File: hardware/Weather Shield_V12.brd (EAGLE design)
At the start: 53.3 x 59.7 mm, 52 parts, among them J1 GP-735, Q1 200mA/50V, Q2 200mA/50V, U1 ARDUINO_R3_SHIELD, U3 ALS-PT19, U4 MPL3115A2LGA8, U5 SI7021, U6 3.3V/150mA

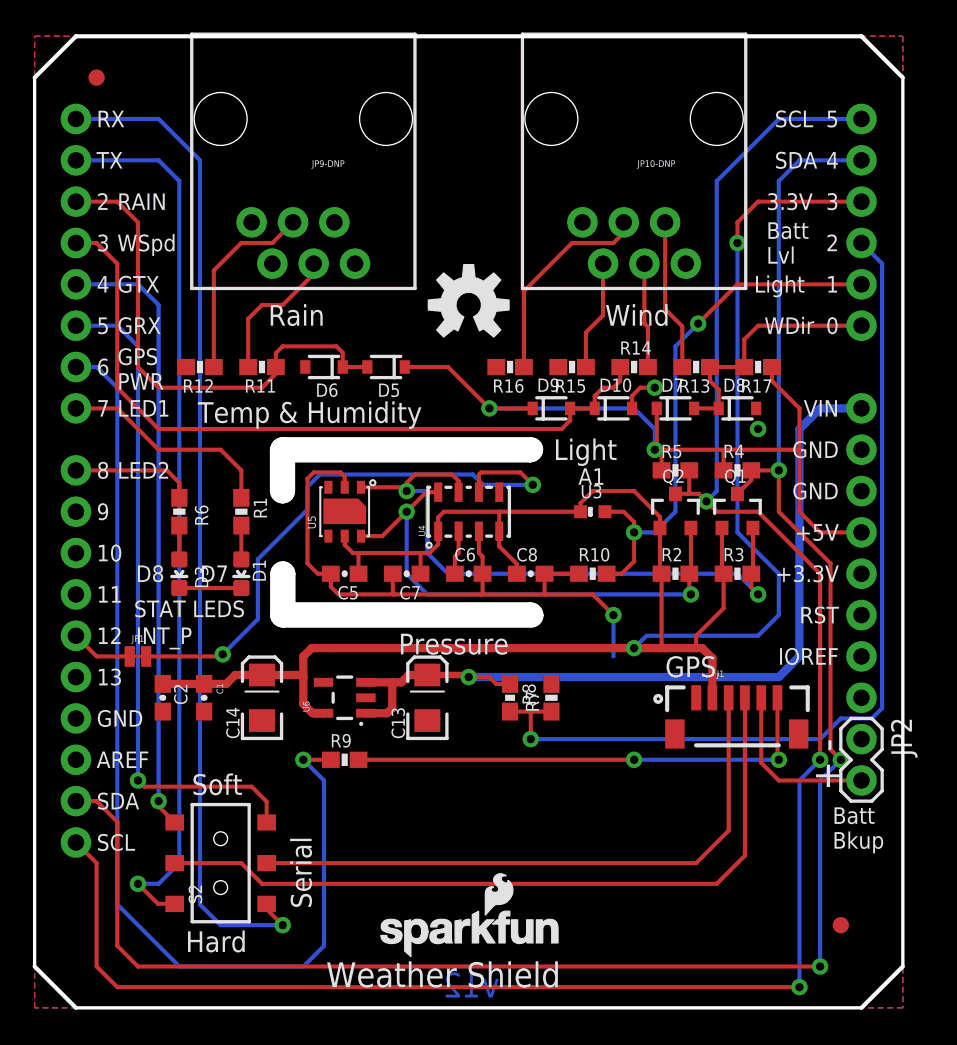
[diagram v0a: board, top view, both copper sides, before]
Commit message: Slight modifications before final review
Moved logos to avoid cover up by GPS. Moved GPS backup batter
connection. Change jumper on D12 to NO instead of NC.
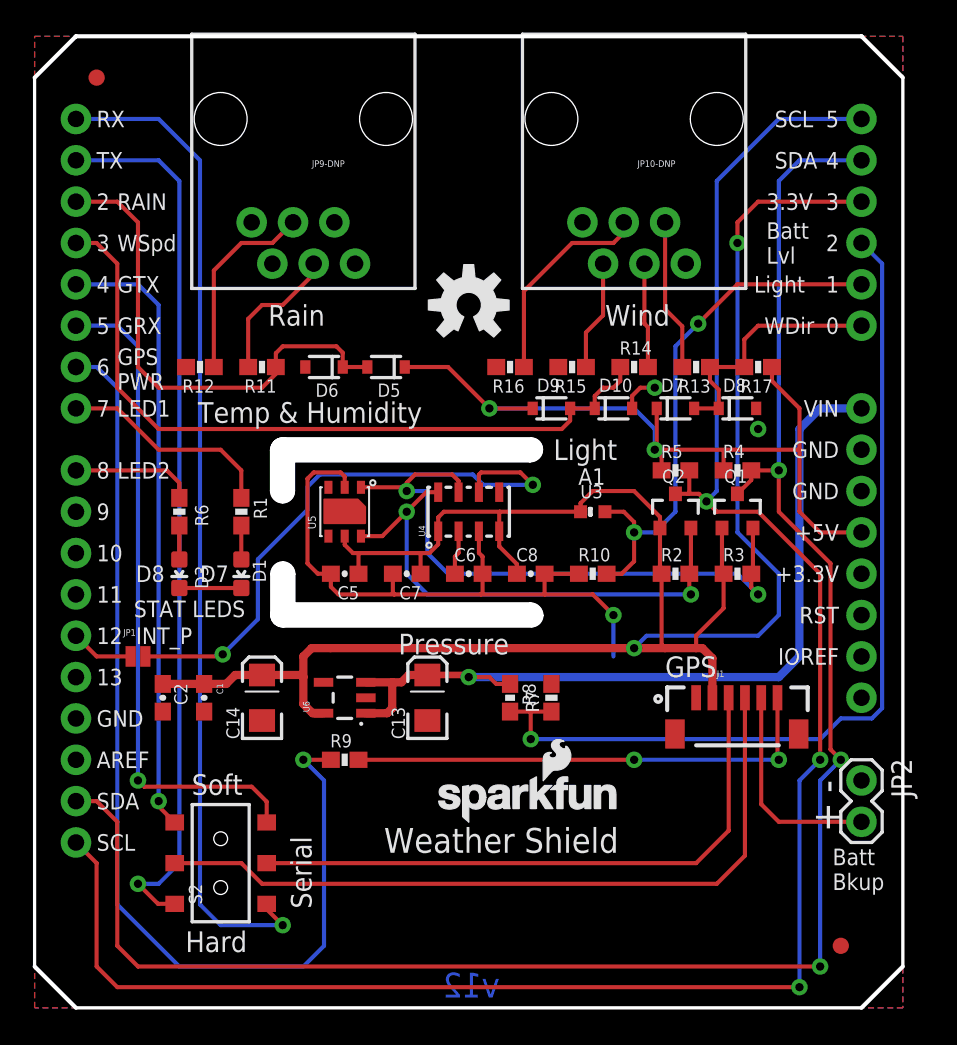
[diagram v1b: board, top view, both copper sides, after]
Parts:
- JP1: value (none) -> JUMPER-PAD-2-NO; device SparkFun-Passives:PAD-JUMPER-2-NC_BY_TRACE_NO_SILK -> SparkFun-Passives:PAD-JUMPER-2-NO_NO_SILK
- moved LOGO2 8.99 mm to (24.4, 11.3)
- moved JP2 2.54 mm to (50.8, 14.0)
- moved FD1 1.27 mm to (49.5, 3.81)
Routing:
- net V_BATT: track 10.6 -> 13.1 mm
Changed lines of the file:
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@@
 <layer number="29" name="tStop" color="7" fill="3" visible="yes" active="yes"/>
 <layer number="30" name="bStop" color="7" fill="6" visible="no" active="yes"/>
-<layer number="31" name="tCream" color="7" fill="4" visible="no" active="yes"/>
+<layer number="31" name="tCream" color="7" fill="4" visible="yes" active="yes"/>
 <layer number="32" name="bCream" color="7" fill="5" visible="no" active="yes"/>
 <layer number="33" name="tFinish" color="6" fill="3" visible="no" active="yes"/>
@@
 <layer number="47" name="Measures" color="7" fill="1" visible="no" active="yes"/>
 <layer number="48" name="Document" color="7" fill="1" visible="no" active="yes"/>
-<layer number="49" name="Reference" color="7" fill="1" visible="no" active="yes"/>
+<layer number="49" name="Reference" color="7" fill="1" visible="yes" active="yes"/>
 <layer number="50" name="dxf" color="7" fill="1" visible="no" active="yes"/>
 <layer number="51" name="tDocu" color="6" fill="1" visible="yes" active="yes"/>
@@
 <wire x1="53.34" y1="2.54" x2="53.34" y2="57.15" width="0.2032" layer="20"/>
 <wire x1="0" y1="57.15" x2="0" y2="2.54" width="0.2032" layer="20"/>
-<text x="17.907" y="1.27" size="1.524" layer="21" font="vector" ratio="15">Weather Shield</text>
+<text x="21.463" y="9.525" size="1.524" layer="21" font="vector" ratio="15">Weather Shield</text>
 <text x="22.86" y="-24.13" size="1.778" layer="51" font="vector" ratio="15">N. Seidle</text>
 <text x="22.352" y="21.717" size="1.27" layer="21" font="vector" ratio="15">Pressure</text>
@@
 <rectangle x1="12.7" y1="22.86" x2="39.37" y2="35.56" layer="41"/>
 <rectangle x1="12.7" y1="22.86" x2="39.37" y2="35.56" layer="42"/>
-<text x="49.022" y="9.779" size="1.016" layer="21" font="vector" ratio="15">Batt
+<text x="49.022" y="7.239" size="1.016" layer="21" font="vector" ratio="15">Batt
 Bkup</text>
-<text x="49.53" y="13.335" size="1.778" layer="21" font="vector" ratio="15" rot="R90">+</text>
-<text x="49.53" y="15.748" size="1.778" layer="21" font="vector" ratio="15" rot="R90">-</text>
+<text x="49.53" y="10.795" size="1.778" layer="21" font="vector" ratio="15" rot="R90">+</text>
+<text x="49.53" y="13.208" size="1.778" layer="21" font="vector" ratio="15" rot="R90">-</text>
 <wire x1="15.24" y1="31.75" x2="15.24" y2="34.29" width="1.524" layer="46"/>
 <wire x1="15.24" y1="34.29" x2="30.48" y2="34.29" width="1.524" layer="46"/>
@@
 <attribute name="PROD_ID" value="RES-07856" x="29.21" y="39.37" size="1.778" layer="27" rot="R180" display="off"/>
 </element>
-<element name="LOGO2" library="SparkFun-Aesthetics" package="SFE_LOGO_NAME_FLAME_.1" value="SFE_LOGO_NAME_FLAME.1_INCH" x="20.828" y="3.048"/>
+<element name="LOGO2" library="SparkFun-Aesthetics" package="SFE_LOGO_NAME_FLAME_.1" value="SFE_LOGO_NAME_FLAME.1_INCH" x="24.384" y="11.303"/>
 <element name="R7" library="SparkFun-Resistors" package="0603-RES" value="1K" x="31.75" y="19.05" smashed="yes" rot="R90">
 <attribute name="NAME" x="30.988" y="18.161" size="0.8128" layer="25" font="vector" rot="R90"/>
@@
 <attribute name="PROD_ID" value="RES-07857" x="19.05" y="15.24" size="1.778" layer="27" display="off"/>
 </element>
-<element name="JP2" library="SparkFun-Connectors" package="1X02" value="External Batt Bckup" x="50.8" y="16.51" rot="R270"/>
+<element name="JP2" library="SparkFun-Connectors" package="1X02" value="External Batt Bckup" x="50.8" y="13.97" rot="R270"/>
 <element name="U3" library="SparkFun-Sensors" package="ALS-PT19" value="ALS-PT19" x="34.29" y="30.48" smashed="yes">
 <attribute name="NAME" x="33.528" y="31.3055" size="0.8128" layer="25"/>
@@
 </element>
 <element name="U$2" library="SparkFun-Aesthetics" package="REVISION" value="REVISION" x="2.54" y="-27.94"/>
-<element name="FD1" library="SparkFun-Aesthetics" package="FIDUCIAL-1X2" value="FIDUCIAL1X2" x="49.53" y="5.08"/>
+<element name="FD1" library="SparkFun-Aesthetics" package="FIDUCIAL-1X2" value="FIDUCIAL1X2" x="49.53" y="3.81"/>
 <element name="FD2" library="SparkFun-Aesthetics" package="FIDUCIAL-1X2" value="FIDUCIAL1X2" x="3.81" y="57.15"/>
-<element name="JP1" library="SparkFun-Passives" package="PAD-JUMPER-2-NC_BY_TRACE_NO_SILK" value="" x="6.35" y="21.59"/>
+<element name="JP1" library="SparkFun-Passives" package="PAD-JUMPER-2-NO_NO_SILK" value="JUMPER-PAD-2-NO" x="6.35" y="21.59"/>
 <element name="U6" library="SparkFun-PowerIC" package="SOT23-5" value="3.3V/150mA" x="19.05" y="19.05" rot="R90">
 <attribute name="PROD_ID" value="VREG-00822" x="19.05" y="19.05" size="1.778" layer="27" font="vector" ratio="15" rot="R90" display="off"/>
@@
 <contactref element="JP1" pad="2"/>
 <wire x1="11.557" y1="21.717" x2="11.43" y2="21.59" width="0.254" layer="1"/>
-<wire x1="11.43" y1="21.59" x2="6.858" y2="21.59" width="0.254" layer="1"/>
+<wire x1="11.43" y1="21.59" x2="6.8" y2="21.59" width="0.254" layer="1"/>
 </signal>
 <signal name="N$5">
@@
 <contactref element="JP2" pad="2"/>
 <contactref element="J1" pad="5"/>
-<wire x1="44.64" y1="19.05" x2="44.64" y2="15.05" width="0.254" layer="1"/>
-<wire x1="44.64" y1="15.05" x2="45.72" y2="13.97" width="0.254" layer="1"/>
-<wire x1="45.72" y1="13.97" x2="50.8" y2="13.97" width="0.254" layer="1"/>
+<wire x1="44.64" y1="19.05" x2="44.64" y2="12.51" width="0.254" layer="1"/>
+<wire x1="50.8" y1="11.43" x2="45.72" y2="11.43" width="0.254" layer="1"/>
+<wire x1="45.72" y1="11.43" x2="44.64" y2="12.51" width="0.254" layer="1"/>
 </signal>
 <signal name="LIGHT">
@@
 <contactref element="U1" pad="D12"/>
 <contactref element="JP1" pad="1"/>
-<wire x1="5.842" y1="21.59" x2="3.81" y2="21.59" width="0.254" layer="1"/>
+<wire x1="5.9" y1="21.59" x2="3.81" y2="21.59" width="0.254" layer="1"/>
 <wire x1="3.81" y1="21.59" x2="2.54" y2="22.86" width="0.254" layer="1"/>
 </signal>

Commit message: Moved logo
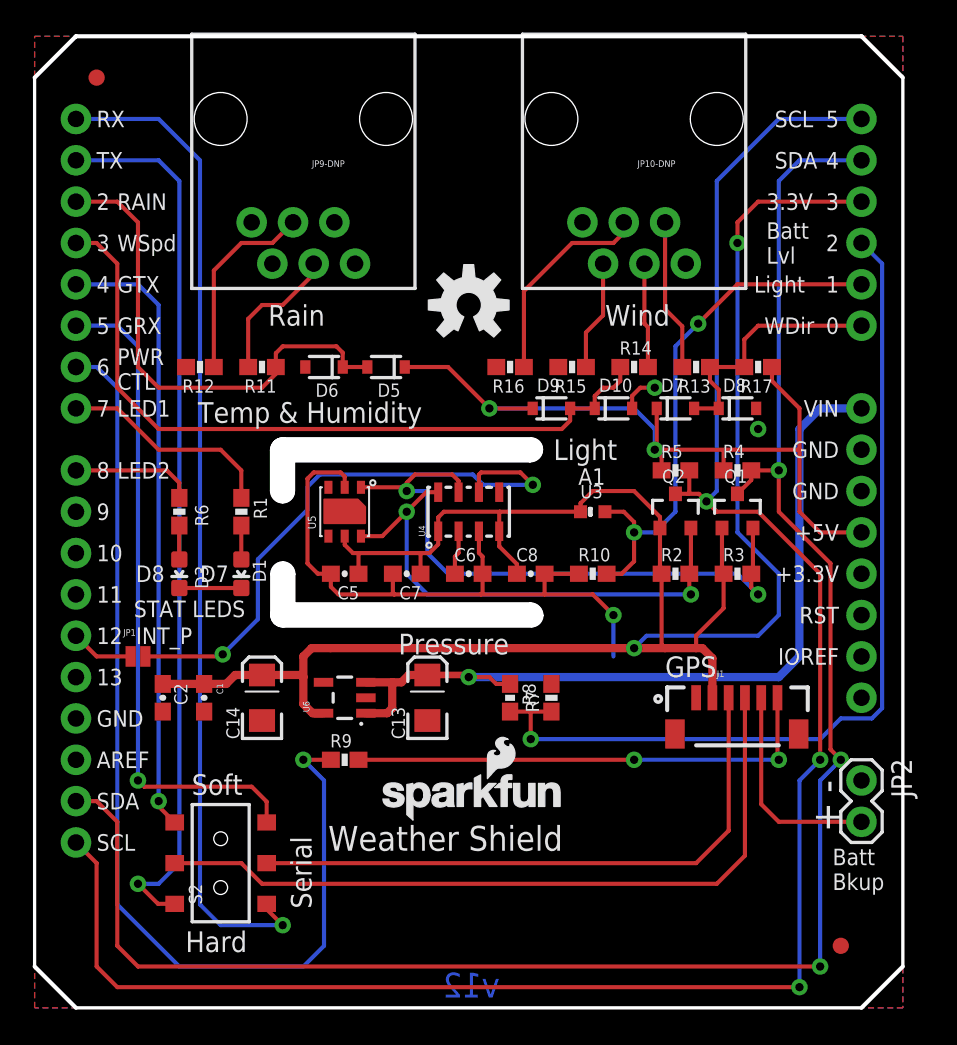
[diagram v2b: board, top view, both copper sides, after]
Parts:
- moved LOGO2 3.43 mm to (21.0, 11.4)
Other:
- board text added: "PWR CTL"
- board text removed: "GPS PWR"
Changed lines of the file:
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@@
 <wire x1="53.34" y1="2.54" x2="53.34" y2="57.15" width="0.2032" layer="20"/>
 <wire x1="0" y1="57.15" x2="0" y2="2.54" width="0.2032" layer="20"/>
-<text x="21.463" y="9.525" size="1.524" layer="21" font="vector" ratio="15">Weather Shield</text>
+<text x="18.034" y="9.652" size="1.524" layer="21" font="vector" ratio="15">Weather Shield</text>
 <text x="22.86" y="-24.13" size="1.778" layer="51" font="vector" ratio="15">N. Seidle</text>
 <text x="22.352" y="21.717" size="1.27" layer="21" font="vector" ratio="15">Pressure</text>
@@
 <text x="6.223" y="26.162" size="1.016" layer="21" font="vector" ratio="15">D8</text>
 <text x="10.16" y="26.162" size="1.016" layer="21" font="vector" ratio="15">D7</text>
-<text x="5.08" y="37.973" size="1.016" layer="21" font="vector" ratio="15">GPS
-PWR</text>
+<text x="5.08" y="37.973" size="1.016" layer="21" font="vector" ratio="15">PWR
+CTL</text>
 <text x="5.08" y="41.402" size="1.016" layer="21" font="vector" ratio="15">GRX</text>
 <text x="5.08" y="43.942" size="1.016" layer="21" font="vector" ratio="15">GTX</text>
@@
 <attribute name="PROD_ID" value="RES-07856" x="29.21" y="39.37" size="1.778" layer="27" rot="R180" display="off"/>
 </element>
-<element name="LOGO2" library="SparkFun-Aesthetics" package="SFE_LOGO_NAME_FLAME_.1" value="SFE_LOGO_NAME_FLAME.1_INCH" x="24.384" y="11.303"/>
+<element name="LOGO2" library="SparkFun-Aesthetics" package="SFE_LOGO_NAME_FLAME_.1" value="SFE_LOGO_NAME_FLAME.1_INCH" x="20.955" y="11.43"/>
 <element name="R7" library="SparkFun-Resistors" package="0603-RES" value="1K" x="31.75" y="19.05" smashed="yes" rot="R90">
 <attribute name="NAME" x="30.988" y="18.161" size="0.8128" layer="25" font="vector" rot="R90"/>

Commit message: Minor Changes after group review for Reds
Fixed text under VREG to have correct info, fixed Eagle error on J1
(GPS Conn), fixed overlapping values, minor silk changes, moved via,
updated HW/SW serial switch text to modern standard .
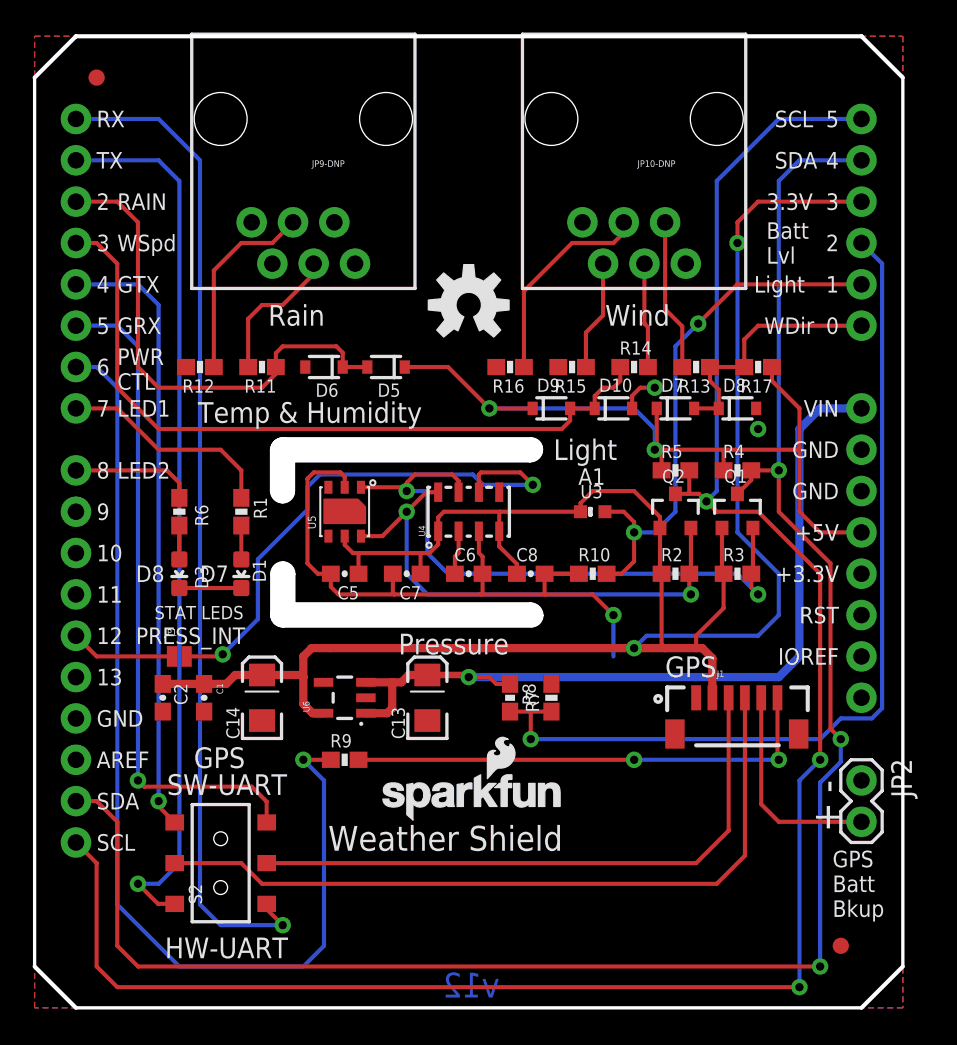
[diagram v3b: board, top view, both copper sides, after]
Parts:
- D10, D5, D6, D7, D8, D9: value 250mA/100V -> (none)
- JP1: value JUMPER-PAD-2-NO -> (none)
- moved JP1 2.54 mm to (8.89, 21.6)
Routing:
- net INT-PRESSURE: track 36.4 -> 33.9 mm
- net N$6: track 3.89 -> 6.43 mm
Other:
- board text added: "GPS Batt Bkup"
- board text added: "HW-UART"
- board text added: "PRESS_INT"
- board text added: "SW-UART"
- board text removed: "Batt Bkup"
- board text removed: "Hard"
- board text removed: "INT_P"
- board text removed: "Serial"
- board text removed: "Soft"

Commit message: Final issue fixes before going out for reds.
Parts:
- D10, D5, D6, D7, D8, D9: value (none) -> 250mA/100V
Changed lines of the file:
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@@
 <text x="38.735" y="20.32" size="1.27" layer="21" font="vector" ratio="15">GPS</text>
 <wire x1="2.54" y1="0" x2="50.8" y2="0" width="0.2032" layer="20"/>
-<wire x1="0" y1="57.15" x2="2.54" y2="59.69" width="0.254" layer="20"/>
-<wire x1="2.54" y1="59.69" x2="50.8" y2="59.69" width="0.254" layer="20"/>
-<wire x1="50.8" y1="59.69" x2="53.34" y2="57.15" width="0.254" layer="20"/>
-<wire x1="53.34" y1="2.54" x2="50.8" y2="0" width="0.254" layer="20"/>
-<wire x1="2.54" y1="0" x2="0" y2="2.54" width="0.254" layer="20"/>
+<wire x1="0" y1="57.15" x2="2.54" y2="59.69" width="0.2032" layer="20"/>
+<wire x1="2.54" y1="59.69" x2="50.8" y2="59.69" width="0.2032" layer="20"/>
+<wire x1="50.8" y1="59.69" x2="53.34" y2="57.15" width="0.2032" layer="20"/>
+<wire x1="53.34" y1="2.54" x2="50.8" y2="0" width="0.2032" layer="20"/>
+<wire x1="2.54" y1="0" x2="0" y2="2.54" width="0.2032" layer="20"/>
 <text x="14.351" y="41.91" size="1.27" layer="21" font="vector" ratio="15">Rain</text>
 <text x="35.052" y="41.91" size="1.27" layer="21" font="vector" ratio="15">Wind</text>
@@
 <attribute name="PROD_ID" value="RES-07856" x="40.64" y="39.37" size="1.778" layer="27" rot="R180" display="off"/>
 </element>
-<element name="D9" library="SparkFun-DiscreteSemi" package="SOD-323" value="" x="31.75" y="36.83" smashed="yes">
+<element name="D9" library="SparkFun-DiscreteSemi" package="SOD-323" value="250mA/100V" x="31.75" y="36.83" smashed="yes">
 <attribute name="NAME" x="30.861" y="37.846" size="0.8128" layer="25"/>
 <attribute name="VALUE" value="250mA/100V" x="30.734" y="35.433" size="0.8128" layer="27"/>
 <attribute name="PROD_ID" value="DIO-09646" x="31.75" y="36.83" size="1.778" layer="27" display="off"/>
 </element>
-<element name="D10" library="SparkFun-DiscreteSemi" package="SOD-323" value="" x="35.56" y="36.83" smashed="yes">
+<element name="D10" library="SparkFun-DiscreteSemi" package="SOD-323" value="250mA/100V" x="35.56" y="36.83" smashed="yes">
 <attribute name="NAME" x="34.671" y="37.846" size="0.8128" layer="25"/>
 <attribute name="VALUE" value="250mA/100V" x="34.544" y="35.433" size="0.8128" layer="27"/>
 <attribute name="PROD_ID" value="DIO-09646" x="35.56" y="36.83" size="1.778" layer="27" display="off"/>
 </element>
-<element name="D7" library="SparkFun-DiscreteSemi" package="SOD-323" value="" x="39.37" y="36.83" smashed="yes">
+<element name="D7" library="SparkFun-DiscreteSemi" package="SOD-323" value="250mA/100V" x="39.37" y="36.83" smashed="yes">
 <attribute name="NAME" x="38.481" y="37.846" size="0.8128" layer="25"/>
 <attribute name="VALUE" value="250mA/100V" x="38.354" y="35.433" size="0.8128" layer="27"/>
 <attribute name="PROD_ID" value="DIO-09646" x="39.37" y="36.83" size="1.778" layer="27" display="off"/>
 </element>
-<element name="D8" library="SparkFun-DiscreteSemi" package="SOD-323" value="" x="43.18" y="36.83" smashed="yes">
+<element name="D8" library="SparkFun-DiscreteSemi" package="SOD-323" value="250mA/100V" x="43.18" y="36.83" smashed="yes">
 <attribute name="NAME" x="42.291" y="37.846" size="0.8128" layer="25"/>
 <attribute name="VALUE" value="250mA/100V" x="42.164" y="35.433" size="0.8128" layer="27"/>
 <attribute name="PROD_ID" value="DIO-09646" x="43.18" y="36.83" size="1.778" layer="27" display="off"/>
 </element>
-<element name="D5" library="SparkFun-DiscreteSemi" package="SOD-323" value="" x="21.59" y="39.37" smashed="yes" rot="R180">
+<element name="D5" library="SparkFun-DiscreteSemi" package="SOD-323" value="250mA/100V" x="21.59" y="39.37" smashed="yes" rot="R180">
 <attribute name="NAME" x="22.479" y="38.354" size="0.8128" layer="25" rot="R180"/>
 <attribute name="VALUE" value="250mA/100V" x="22.606" y="40.767" size="0.8128" layer="27" rot="R180"/>
 <attribute name="PROD_ID" value="DIO-09646" x="21.59" y="39.37" size="1.778" layer="27" rot="R180" display="off"/>
 </element>
-<element name="D6" library="SparkFun-DiscreteSemi" package="SOD-323" value="" x="17.78" y="39.37" smashed="yes" rot="R180">
+<element name="D6" library="SparkFun-DiscreteSemi" package="SOD-323" value="250mA/100V" x="17.78" y="39.37" smashed="yes" rot="R180">
 <attribute name="NAME" x="18.669" y="38.354" size="0.8128" layer="25" rot="R180"/>
 <attribute name="VALUE" value="250mA/100V" x="18.796" y="40.767" size="0.8128" layer="27" rot="R180"/>
